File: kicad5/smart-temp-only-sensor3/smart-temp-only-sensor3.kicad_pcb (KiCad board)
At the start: 2 copper layers, 2 parts, among them J1 USB_B_Mini, J2 Conn_01x04_Female

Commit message: noid: autoroute final beta
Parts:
- J1: footprint Connector_USB:USB_A_Molex_67643_Horizontal -> Connector_USB:USB_Mini-B_Tensility_54-00023_Vertical
- J2: footprint Connector_PinHeader_2.54mm:PinHeader_1x04_P2.54mm_Vertical -> Connector_PinSocket_2.54mm:PinSocket_1x04_P2.54mm_Vertical
- moved J2 13.5 mm to (76.8, 60.3)
- moved J1 6.79 mm to (82.2, 62.5)
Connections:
- J1 pad 1: Net-(J1-Pad1) -> +3V3
- J1 pad 5: Net-(J1-Pad5) -> GND1
- J2 pad 1: Net-(J2-Pad1) -> +3V3
- J2 pad 2: Net-(J2-Pad2) -> Net-(J1-Pad3)
- J2 pad 3: Net-(J2-Pad3) -> Net-(J1-Pad2)
- J2 pad 4: Net-(J2-Pad4) -> GND1
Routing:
- net Net-(J1-Pad6): track 0.00 -> 10.5 mm
- net Net-(J1-Pad2): track 0.00 -> 9.92 mm
- net GND1: track 0.00 -> 6.35 mm
- net +3V3: track 0.00 -> 6.33 mm
- net Net-(J1-Pad3): track 0.00 -> 5.94 mm
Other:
- board outline added: 18 x 12.2 mm

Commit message: smart-temp-only-sensor3
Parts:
- J1: footprint Connector_USB:USB_Mini-B_Tensility_54-00023_Vertical -> kicad3_footprint:USB_Mini-B_econ_connect_vertical
- J2: value Conn_01x04_Female -> Conn_Female
- moved J1 12.2 mm to (91.1, 70.9)
- moved J2 10.9 mm to (83.9, 68.6)
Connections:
- J1 pad 2: Net-(J1-Pad2) -> /SDA_GPIO_0
- J1 pad 3: Net-(J1-Pad3) -> /SDL_GPIO_2
- J2 pad 2: Net-(J1-Pad3) -> GND1
- J2 pad 3: Net-(J1-Pad2) -> /SDL_GPIO_2
- J2 pad 4: GND1 -> /SDA_GPIO_0
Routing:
- net /SDA_GPIO_0: track 0.00 -> 13.1 mm
- net Net-(J1-Pad2): track 9.92 -> 0.00 mm
- net Net-(J1-Pad6): track 10.5 -> 19.2 mm
- net /SDL_GPIO_2: track 0.00 -> 7.61 mm
- net GND1: track 6.35 -> 12.7 mm
- net Net-(J1-Pad3): track 5.94 -> 0.00 mm
- net +3V3: track 6.33 -> 8.08 mm
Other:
- board size 18 x 12.2 mm -> 17.8 x 12.7 mm

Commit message: double check conn
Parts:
- J2: value Conn_Female -> Conn_01x04_Female
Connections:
- J1 pad 2: /SDA_GPIO_0 -> /SDL_GPIO_2-
- J1 pad 3: /SDL_GPIO_2 -> Net-(J1-Pad3)
- J2 pad 3: /SDL_GPIO_2 -> /SDL_GPIO_2-
- J2 pad 4: /SDA_GPIO_0 -> Net-(J1-Pad3)
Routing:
- net /SDA_GPIO_0: track 13.1 -> 0.00 mm
- net GND1: track 12.7 -> 0.00 mm
- net Net-(J1-Pad6): track 19.2 -> 10.4 mm
- net +3V3: track 8.08 -> 0.00 mm
- net /SDL_GPIO_2: track 7.61 -> 0.00 mm
- net Net-(J1-Pad3): track 0.00 -> 2.13 mm
- net /SDL_GPIO_2-: track 0.00 -> 0.61 mm
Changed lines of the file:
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@@
     (thickness 1.6)
     (drawings 14)
-    (tracks 25)
+    (tracks 6)
     (zones 0)
     (modules 2)
@@
   (net 3 +3V3)
   (net 4 GND1)
-  (net 5 /SDA_GPIO_0)
-  (net 6 /SDL_GPIO_2)
+  (net 5 "Net-(J1-Pad3)")
+  (net 6 /SDL_GPIO_2-)
   (net_class Default "This is the default net class."
     (clearance 0.2)
@@
     (uvia_drill 0.1)
     (add_net +3V3)
-    (add_net /SDA_GPIO_0)
-    (add_net /SDL_GPIO_2)
+    (add_net /SDL_GPIO_2-)
     (add_net GND1)
+    (add_net "Net-(J1-Pad3)")
     (add_net "Net-(J1-Pad4)")
     (add_net "Net-(J1-Pad6)")
@@
       (net 1 "Net-(J1-Pad4)"))
     (pad 3 thru_hole circle (at 1.6 0 270) (size 1.1 1.1) (drill 0.7) (layers *.Cu *.Mask)
-      (net 6 /SDL_GPIO_2))
+      (net 5 "Net-(J1-Pad3)"))
     (pad 2 thru_hole circle (at 0.8 -1.75 270) (size 1.1 1.1) (drill 0.7) (layers *.Cu *.Mask)
-      (net 5 /SDA_GPIO_0))
+      (net 6 /SDL_GPIO_2-))
     (pad 1 thru_hole rect (at 0 0 270) (size 1.1 1.1) (drill 0.7) (layers *.Cu *.Mask)
       (net 3 +3V3))
@@
       (effects (font (size 1 1) (thickness 0.15)))
     )
-    (fp_text value Conn_Female (at 2.54 4.445 90) (layer F.Fab)
+    (fp_text value Conn_01x04_Female (at 6.223 9.525 180) (layer F.Fab)
       (effects (font (size 1 1) (thickness 0.15)))
     )
@@
       (net 4 GND1))
     (pad 3 thru_hole oval (at 0 5.08) (size 1.7 1.7) (drill 1) (layers *.Cu *.Mask)
-      (net 6 /SDL_GPIO_2))
+      (net 6 /SDL_GPIO_2-))
     (pad 4 thru_hole oval (at 0 7.62) (size 1.7 1.7) (drill 1) (layers *.Cu *.Mask)
-      (net 5 /SDA_GPIO_0))
+      (net 5 "Net-(J1-Pad3)"))
     (model ${KISYS3DMOD}/Connector_PinSocket_2.54mm.3dshapes/PinSocket_1x04_P2.54mm_Vertical.wrl
       (at (xyz 0 0 0))
@@
   (gr_line (start 99.06 67.31) (end 99.06 77.47) (layer Edge.Cuts) (width 0.05))
   (gr_line (start 82.55 66.04) (end 97.79 66.04) (layer Edge.Cuts) (width 0.05))
-  (segment (start 96.393 76.134) (end 97.9181 76.134) (width 0.25) (layer B.Cu) (net 2))
-  (segment (start 96.393 68.834) (end 97.9181 68.834) (width 0.25) (layer B.Cu) (net 2))
+  (segment (start 96.393 76.134) (end 97.9181 76.134) (width 0.25) (layer B.Cu) (net 2) (status 10))
+  (segment (start 96.393 68.834) (end 97.9181 68.834) (width 0.25) (layer B.Cu) (net 2) (status 10))
   (segment (start 97.9181 68.834) (end 97.9181 76.134) (width 0.25) (layer B.Cu) (net 2))
-  (segment (start 96.393 68.834) (end 91.948 68.834) (width 0.25) (layer F.Cu) (net 2))
-  (segment (start 96.393 76.134) (end 91.948 76.134) (width 0.25) (layer F.Cu) (net 2))
-  (segment (start 83.947 68.58) (end 85.1221 68.58) (width 0.25) (layer F.Cu) (net 3))
-  (segment (start 85.1221 68.58) (end 87.4261 70.884) (width 0.25) (layer F.Cu) (net 3))
-  (segment (start 87.4261 70.884) (end 91.073 70.884) (width 0.25) (layer F.Cu) (net 3))
-  (segment (start 83.947 71.12) (end 83.947 72.2951) (width 0.25) (layer F.Cu) (net 4))
-  (segment (start 83.947 72.2951) (end 83.5798 72.2951) (width 0.25) (layer F.Cu) (net 4))
-  (segment (start 83.5798 72.2951) (end 82.7643 73.1106) (width 0.25) (layer F.Cu) (net 4))
-  (segment (start 82.7643 73.1106) (end 82.7643 74.1426) (width 0.25) (layer F.Cu) (net 4))
-  (segment (start 82.7643 74.1426) (end 83.4895 74.8678) (width 0.25) (layer F.Cu) (net 4))
-  (segment (start 83.4895 74.8678) (end 85.5325 74.8678) (width 0.25) (layer F.Cu) (net 4))
-  (segment (start 85.5325 74.8678) (end 86.3163 74.084) (width 0.25) (layer F.Cu) (net 4))
-  (segment (start 86.3163 74.084) (end 91.073 74.084) (width 0.25) (layer F.Cu) (net 4))
-  (segment (start 83.947 76.2) (end 85.1221 76.2) (width 0.25) (layer B.Cu) (net 5))
+  (segment (start 83.947 76.2) (end 85.1221 76.2) (width 0.25) (layer B.Cu) (net 5) (status 10))
   (segment (start 85.1221 76.2) (end 85.1221 75.2452) (width 0.25) (layer B.Cu) (net 5))
-  (segment (start 85.1221 75.2452) (end 90.3585 70.0088) (width 0.25) (layer B.Cu) (net 5))
-  (segment (start 90.3585 70.0088) (end 91.7606 70.0088) (width 0.25) (layer B.Cu) (net 5))
-  (segment (start 91.7606 70.0088) (end 92.823 71.0712) (width 0.25) (layer B.Cu) (net 5))
-  (segment (start 92.823 71.0712) (end 92.823 71.684) (width 0.25) (layer B.Cu) (net 5))
-  (segment (start 83.947 73.66) (end 85.1221 73.66) (width 0.25) (layer F.Cu) (net 6))
-  (segment (start 85.1221 73.66) (end 86.2981 72.484) (width 0.25) (layer F.Cu) (net 6))
-  (segment (start 86.2981 72.484) (end 91.073 72.484) (width 0.25) (layer F.Cu) (net 6))
+  (segment (start 92.823 71.0712) (end 92.823 71.684) (width 0.25) (layer B.Cu) (net 6) (status 20))
 )

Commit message: only sensor
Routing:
- net /SDL_GPIO_2-: track 0.61 -> 11.4 mm
- net Net-(J1-Pad6): track 10.4 -> 19.2 mm
- net GND1: track 0.00 -> 8.35 mm
- net +3V3: track 0.00 -> 8.08 mm
- net Net-(J1-Pad3): track 2.13 -> 9.22 mm
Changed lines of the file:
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@@
     (thickness 1.6)
     (drawings 14)
-    (tracks 6)
+    (tracks 21)
     (zones 0)
     (modules 2)
@@
   (gr_line (start 99.06 67.31) (end 99.06 77.47) (layer Edge.Cuts) (width 0.05))
   (gr_line (start 82.55 66.04) (end 97.79 66.04) (layer Edge.Cuts) (width 0.05))
-  (segment (start 96.393 76.134) (end 97.9181 76.134) (width 0.25) (layer B.Cu) (net 2) (status 10))
-  (segment (start 96.393 68.834) (end 97.9181 68.834) (width 0.25) (layer B.Cu) (net 2) (status 10))
+  (segment (start 96.393 68.834) (end 91.948 68.834) (width 0.25) (layer F.Cu) (net 2))
+  (segment (start 96.393 76.134) (end 91.948 76.134) (width 0.25) (layer F.Cu) (net 2))
+  (segment (start 96.393 68.834) (end 97.9181 68.834) (width 0.25) (layer B.Cu) (net 2))
   (segment (start 97.9181 68.834) (end 97.9181 76.134) (width 0.25) (layer B.Cu) (net 2))
-  (segment (start 83.947 76.2) (end 85.1221 76.2) (width 0.25) (layer B.Cu) (net 5) (status 10))
+  (segment (start 97.9181 76.134) (end 96.393 76.134) (width 0.25) (layer B.Cu) (net 2))
+  (segment (start 83.947 68.58) (end 85.1221 68.58) (width 0.25) (layer F.Cu) (net 3))
+  (segment (start 85.1221 68.58) (end 87.4261 70.884) (width 0.25) (layer F.Cu) (net 3))
+  (segment (start 87.4261 70.884) (end 91.073 70.884) (width 0.25) (layer F.Cu) (net 3))
+  (segment (start 83.947 71.12) (end 85.1221 71.12) (width 0.25) (layer F.Cu) (net 4))
+  (segment (start 85.1221 71.12) (end 88.0861 74.084) (width 0.25) (layer F.Cu) (net 4))
+  (segment (start 88.0861 74.084) (end 91.073 74.084) (width 0.25) (layer F.Cu) (net 4))
+  (segment (start 85.1221 75.2452) (end 87.8833 72.484) (width 0.25) (layer B.Cu) (net 5))
+  (segment (start 87.8833 72.484) (end 91.073 72.484) (width 0.25) (layer B.Cu) (net 5))
+  (segment (start 83.947 76.2) (end 85.1221 76.2) (width 0.25) (layer B.Cu) (net 5))
   (segment (start 85.1221 76.2) (end 85.1221 75.2452) (width 0.25) (layer B.Cu) (net 5))
-  (segment (start 92.823 71.0712) (end 92.823 71.684) (width 0.25) (layer B.Cu) (net 6) (status 20))
+  (segment (start 83.947 73.66) (end 85.1221 73.66) (width 0.25) (layer B.Cu) (net 6))
+  (segment (start 92.823 71.0743) (end 91.7575 70.0088) (width 0.25) (layer B.Cu) (net 6))
+  (segment (start 91.7575 70.0088) (end 88.7733 70.0088) (width 0.25) (layer B.Cu) (net 6))
+  (segment (start 88.7733 70.0088) (end 85.1221 73.66) (width 0.25) (layer B.Cu) (net 6))
+  (segment (start 92.823 71.0743) (end 92.823 71.684) (width 0.25) (layer B.Cu) (net 6))
+  (segment (start 92.823 71.0712) (end 92.823 71.0743) (width 0.25) (layer B.Cu) (net 6))
 )

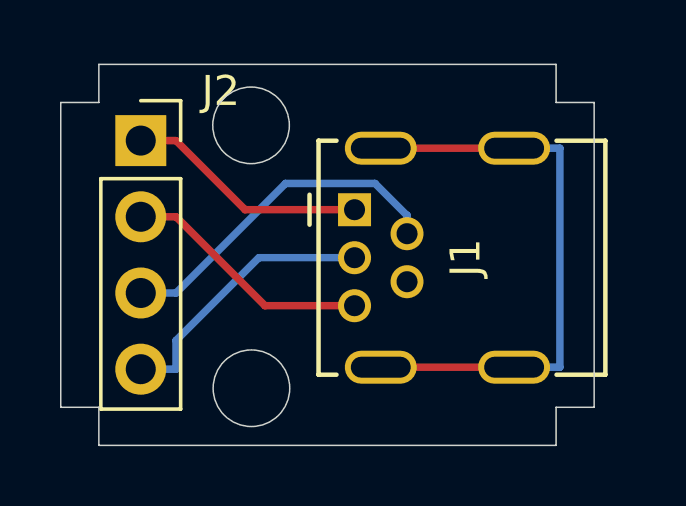
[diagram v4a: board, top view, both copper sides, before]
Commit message: noid: changed female usb connect ids
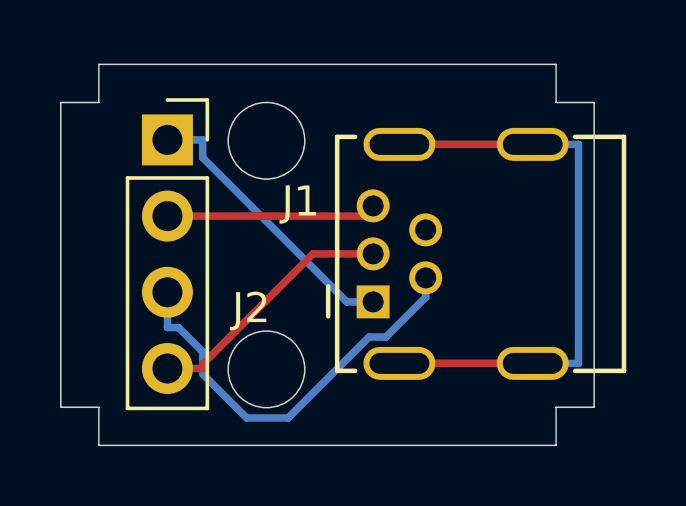
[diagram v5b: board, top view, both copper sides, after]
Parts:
- moved J1 8.11 mm to (99.1, 72.3), turned to 90 degrees
- moved J2 0.89 mm to (84.8, 68.6)
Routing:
- net /SDL_GPIO_2-: track 11.4 -> 13.8 mm
- net +3V3: track 8.08 -> 9.44 mm
- net GND1: track 8.35 -> 7.00 mm
- net Net-(J1-Pad3): track 9.22 -> 8.53 mm
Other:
- outline, holes or cut-outs redrawn
